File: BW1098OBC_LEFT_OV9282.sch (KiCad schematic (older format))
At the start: 39 parts

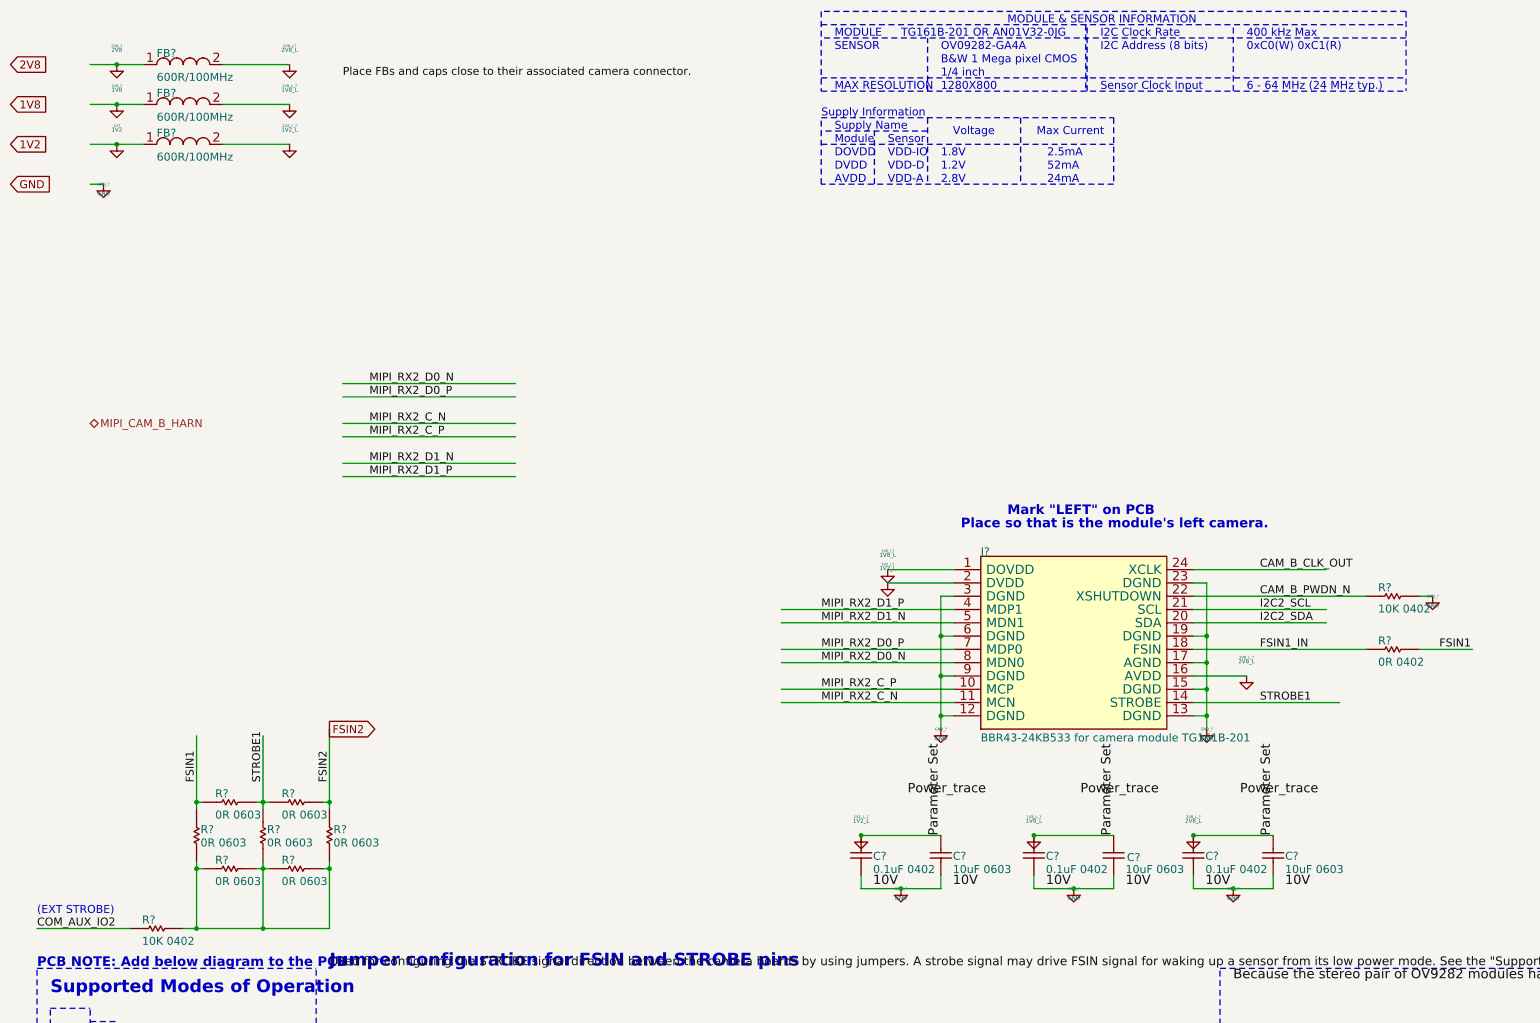
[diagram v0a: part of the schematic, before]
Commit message: More deletion of corrupted or duplicate files, added footprints and associations for mounting holes and 30 pin connector
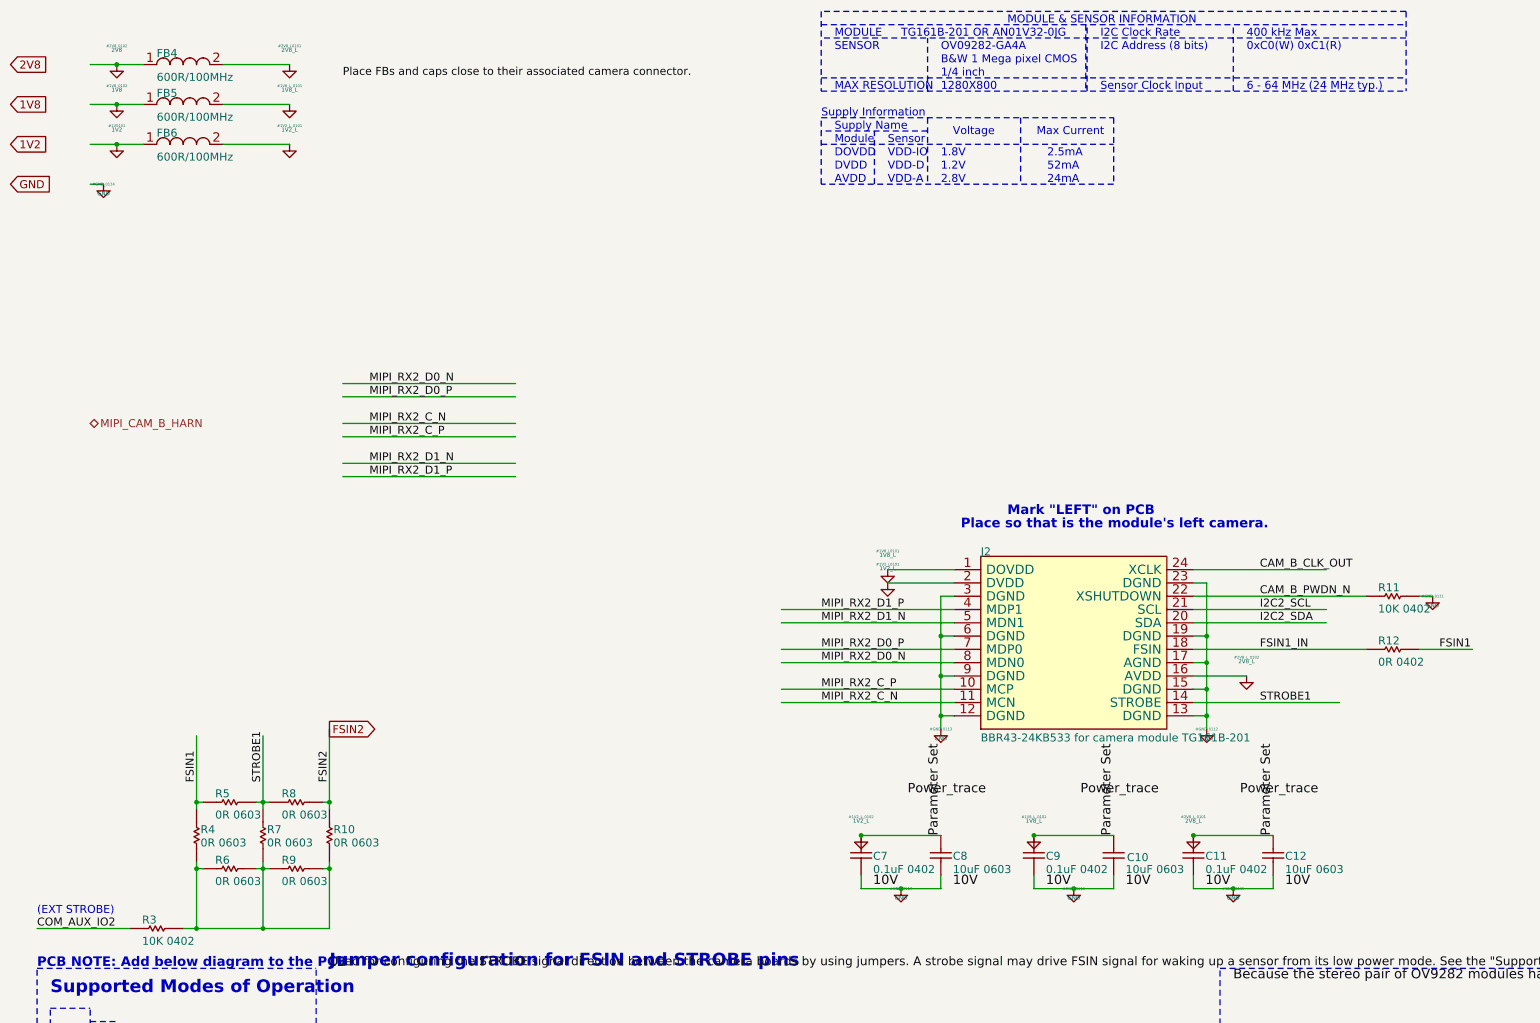
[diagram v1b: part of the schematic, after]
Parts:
- removed 1V2_L?, 1V2_L_? (x2): 1V2_L, symbol power:GND
- removed 1V8_?: 1V8, symbol power:GND
- removed 1V8_L?, 1V8_L_? (x2): 1V8_L, symbol power:GND
- removed 1V?: 1V2, symbol power:GND
- removed 2V8_?: 2V8, symbol power:GND
- removed 2V8_L?, 2V8_L_? (x2): 2V8_L, symbol power:GND
- removed GND_? (x7): GND, symbol power:GND
- gave numbers to parts that had none: 20
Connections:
- net labels added: 1V2_L, 1V8_L, 2V8_L

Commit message: Fixed all LEFT_OV9282 sch nets, need to find datasheet for this last connector to make fp
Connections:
- net labels removed: Because the stereo pair of OV9282 modules hard wired to CAM_B no additional reset cirucitry is required to account for different conditions. This means that "CAM1" (Left) is reset via CAM_PWDN, and "CAM2" (Right), is reset via CAM_PWM. This also means that the signal CAM_AUX_IO1 is no longer required here, as that was only possible if the stereo pair were connected to CAM_C or CAM_D, CTL_CAM_B_HARN, I2C2_HARN, MIPI_CAM_B_HARN, OV9282 sensor I2C address may be changed via I2C protocol. Therefore, in order to assign different I2C address to the sensors on the same I2C bus, one needs to hold the reset the all sensors except one and assign a unique I2C address to the active sensor. This routine should be applied for all sensors in the initialization routine., Place FBs and caps close to their associated camera connector., Used for configuring the STROBE signal direction between the camera boards by using jumpers. A strobe signal may drive FSIN signal for waking up a sensor from its low power mode. See the "Supported Modes of Operation" note for supported jumper settings.      - "NO SYNC" is the mode in which none of the camera modules is excited by any strobe signal.      - "NORMAL" mode means STROBE mechanism works only among the stereo cameras themselves. In this mode, CAM1 strobe is connected to the CAM2 FSIN input.      - "TIMING MASTER" mode means CAM1 STROBE signal drives the EXT_STROBE signal as well as the CAM2 FSIN input. EXT_STROBE signal circulates among the other camera ports so that one camera module can manage the timing of all cameras within the system.     - "TIMING SLAVE" mode uses external strobe signal which is driven externally by another camera. In this mode, CAM1 and CAM2 are excited by the EXT_STROBE signal.    Note that, at most only one camera can be in the "TIMING MASTER" mode at a time. STROBE generation and FSIN reception should be configured via software.
- wire segments 96 -> 87
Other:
- note added: "Because the stereo pair of OV9282 modules hard wired to CAM_B no additional reset cirucitry is \nrequired to account for different conditions. This means that "CAM1" (Left) is reset via \nCAM_PWDN, and "CAM2" (Right), is reset via CAM_PWM. This also means that the signal \nCAM_AUX_IO1 is no longer required here, as that was only possible if the stereo pair were \nconnected to CAM_C or CAM_D"
- note added: "OV9282 sensor I2C address may be changed via I2C protocol. Therefore, in order to assign \ndifferent I2C address to the sensors on the same I2C bus, one needs to hold the reset the all \nsensors except one and assign a unique I2C address to the active sensor. This routine should be \napplied for all sensors in the initialization routine."
- note added: "Place FBs and caps close to \ntheir associated camera connector."
- note added: "Used for configuring the STROBE signal direction between the camera boards by using jumpers. \nA strobe signal may drive FSIN signal for waking up a sensor from its low power mode. See the \n"Supported Modes of Operation" note for supported jumper settings. \n \n - "NO SYNC" is the mode in which none of the camera modules is excited by any strobe signal. \n \n - "NORMAL" mode means STROBE mechani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"
- note removed: "*"
- note removed: "1925 Harmony Park Drive"
- note removed: "4"
- note removed: "8"
- note removed: "80234"
- note removed: "=document_number"
- note removed: "=drawn_by"
- note removed: "=project_title"
- note removed: "=revision"
- note removed: "Date:"
- note removed: "Drawn by:"
- note removed: "Luxonis Holding"
- note removed: "NO SYNC"
- note removed: "NORMAL"
- note removed: "Number:"
- note removed: "PCB NOTE: Add below diagram to the PCB"
- note removed: "Revision:"
- note removed: "Sheet"
- note removed: "Size:"
- note removed: "Supported Modes of Operation"
- note removed: "TIMING MASTER"
- note removed: "TIMING SLAVE"
- note removed: "Tabloid"
- note removed: "Time:"
- note removed: "Title"
- note removed: "United States"
- note removed: "Westminster, CO"
- note removed: "of"
- moved on the sheet: C10, C11, C12, C7, C8, C9, R10, R3, R4, R5, R6, R7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
